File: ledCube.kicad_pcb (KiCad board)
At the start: 2 copper layers, 52 x 22 mm, 13 parts, among them P1 CONN_01X03, P2 CONN_01X02, P3 CONN_01X02, P4 CONN_01X02, P5 CONN_01X02, U1 AL8805W5

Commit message: Generate BOM & Gerber
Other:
- outline, holes or cut-outs redrawn
- board text added: "PWM V+ GND"
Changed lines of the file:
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@@
     (links 22)
     (no_connects 0)
-    (area 118.899999 88.899999 141.100001 111.100001)
+    (area 88.899999 86.925 144.033334 112.175)
     (thickness 1.6)
-    (drawings 14)
+    (drawings 15)
     (tracks 56)
     (zones 0)
@@
     (pad_to_mask_clearance 0.2)
     (aux_axis_origin 0 0)
-    (visible_elements FFFFFF7F)
+    (visible_elements 7FFFFFFF)
     (pcbplotparams
-      (layerselection 0x00030_80000001)
+      (layerselection 0x010f0_80000001)
       (usegerberextensions false)
       (excludeedgelayer true)
@@
       (outputformat 1)
       (mirror false)
-      (drillshape 1)
+      (drillshape 0)
       (scaleselection 1)
-      (outputdirectory ""))
+      (outputdirectory gerber/))
   )
   (net 0 "")
@@
     )
   )
+  (gr_text "PWM V+ GND" (at 133.1 105.3) (layer B.SilkS)
+    (effects (font (size 1 1) (thickness 0.25)) (justify mirror))
+  )
   (gr_text "BlueSink\nLedCube v.0" (at 94.2 105.2) (layer F.SilkS)
     (effects (font (size 1 1) (thickness 0.25) italic))
@@
   (gr_line (start 89 111) (end 111 111) (layer Edge.Cuts) (width 0.2))
   (gr_line (start 89 89) (end 89 111) (layer Edge.Cuts) (width 0.2))
-  (gr_circle (center 100 100) (end 100 96) (layer Edge.Cuts) (width 0.15))
+  (gr_circle (center 100 100) (end 100 95.9) (layer Edge.Cuts) (width 0.15))
   (gr_line (start 89 89) (end 111 89) (layer Edge.Cuts) (width 0.2))
   (gr_line (start 123.75 95) (end 119 95) (layer Edge.Cuts) (width 0.2))

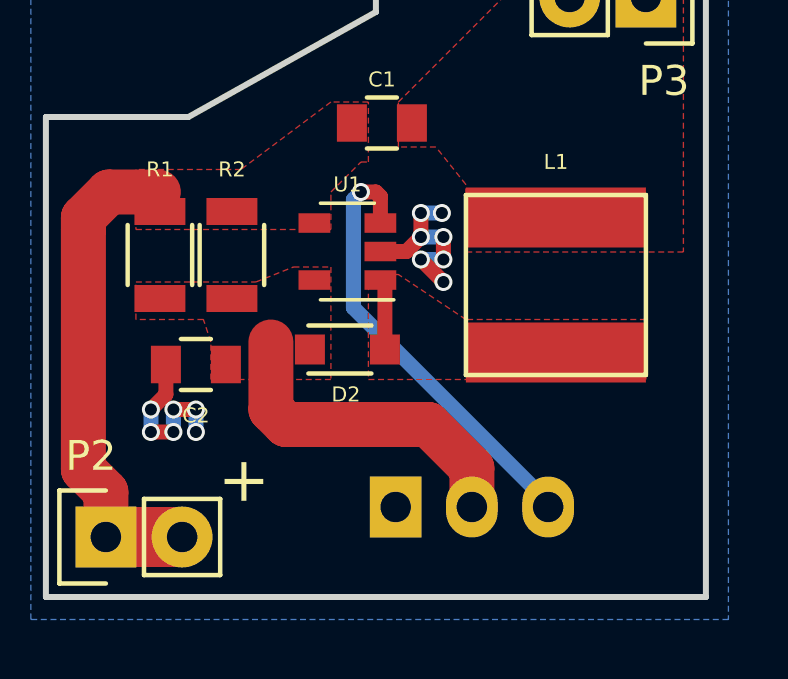
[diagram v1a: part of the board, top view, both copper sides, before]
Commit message: pull down PWM line
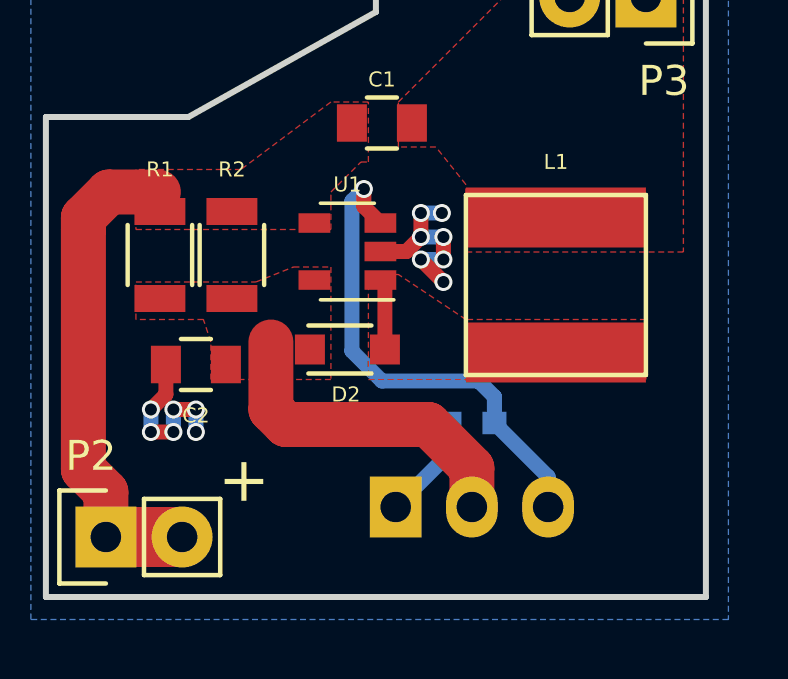
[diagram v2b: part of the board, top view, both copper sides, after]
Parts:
- added R3: 10k, Capacitors_SMD:C_0603, B.Cu at (133.2, 105.2)
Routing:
- net GND: track 11.8 -> 15.4 mm
- net /PWM: track 14.9 -> 16.9 mm
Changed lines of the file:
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@@
-(kicad_pcb (version 4) (host pcbnew 4.0.4-stable)
+(kicad_pcb (version 20160815) (host pcbnew "(2016-12-22 revision d365dc5)-makepkg")
   (general
-    (links 22)
+    (links 24)
     (no_connects 0)
-    (area 88.899999 86.925 144.033334 112.175)
+    (area 88.899999 88.899999 141.100001 111.100001)
     (thickness 1.6)
     (drawings 15)
-    (tracks 56)
+    (tracks 62)
     (zones 0)
-    (modules 13)
+    (modules 14)
     (nets 9)
   )
   (page A4)
   (layers
-    (0 F.Cu signal)
-    (31 B.Cu signal)
+    (0 F.Cu signal hide)
+    (31 B.Cu signal hide)
     (32 B.Adhes user)
     (33 F.Adhes user)
@@
       (hpglpenspeed 20)
       (hpglpendiameter 15)
-      (hpglpenoverlay 2)
       (psnegative false)
       (psa4output false)
@@
     (uvia_dia 0.3)
     (uvia_drill 0.1)
+    (diff_pair_gap 0.25)
+    (diff_pair_width 0.2)
     (add_net /LED+/L)
     (add_net /LED+/U)
@@
   (module footprint:inductor_33uH (layer F.Cu)
     (at 136 100.6 270)
-    (fp_text reference L1 (at -4.1 0 360) (layer F.SilkS)
+    (fp_text reference L1 (at -4.1 0) (layer F.SilkS)
       (effects (font (size 0.5 0.5) (thickness 0.125)))
     )
@@
     )
   )
-  (gr_text "PWM V+ GND" (at 133.1 105.3) (layer B.SilkS)
+  (module Capacitors_SMD:C_0603 (layer B.Cu)
+    (at 133.2 105.2 180)
+    (descr "Capacitor SMD 0603, reflow soldering, AVX (see smccp.pdf)")
+    (tags "capacitor 0603")
+    (attr smd)
+    (fp_text reference R3 (at 0 1.4 180) (layer B.SilkS)
+      (effects (font (size 0.5 0.5) (thickness 0.125)) (justify mirror))
+    )
+    (fp_text value 10k (at 0 -1.9 180) (layer B.Fab) hide
+      (effects (font (size 1 1) (thickness 0.15)) (justify mirror))
+    )
+    (fp_line (start 0.35 -0.6) (end -0.35 -0.6) (layer B.SilkS) (width 0.15))
+    (fp_line (start -0.35 0.6) (end 0.35 0.6) (layer B.SilkS) (width 0.15))
+    (fp_line (start 1.45 0.75) (end 1.45 -0.75) (layer B.CrtYd) (width 0.05))
+    (fp_line (start -1.45 0.75) (end -1.45 -0.75) (layer B.CrtYd) (width 0.05))
+    (fp_line (start -1.45 -0.75) (end 1.45 -0.75) (layer B.CrtYd) (width 0.05))
+    (fp_line (start -1.45 0.75) (end 1.45 0.75) (layer B.CrtYd) (width 0.05))
+    (fp_line (start -0.8 0.4) (end 0.8 0.4) (layer B.Fab) (width 0.15))
+    (fp_line (start 0.8 0.4) (end 0.8 -0.4) (layer B.Fab) (width 0.15))
+    (fp_line (start 0.8 -0.4) (end -0.8 -0.4) (layer B.Fab) (width 0.15))
+    (fp_line (start -0.8 -0.4) (end -0.8 0.4) (layer B.Fab) (width 0.15))
+    (pad 2 smd rect (at 0.75 0 180) (size 0.8 0.75) (layers B.Cu B.Paste B.Mask)
+      (net 2 GND))
+    (pad 1 smd rect (at -0.75 0 180) (size 0.8 0.75) (layers B.Cu B.Paste B.Mask)
+      (net 4 /PWM))
+    (model Capacitors_SMD.3dshapes/C_0603.wrl
+      (at (xyz 0 0 0))
+      (scale (xyz 1 1 1))
+      (rotate (xyz 0 0 0))
+    )
+  )
+  (gr_text "PWM V+ GND" (at 133 110.2) (layer B.SilkS)
     (effects (font (size 1 1) (thickness 0.25)) (justify mirror))
   )
@@
   (segment (start 133.2 106.7) (end 131.75 105.25) (width 1.5) (layer F.Cu) (net 1))
   (segment (start 133.2 108) (end 133.2 106.7) (width 1.5) (layer F.Cu) (net 1))
+  (segment (start 132.45 105.2) (end 132.45 106.21) (width 0.5) (layer B.Cu) (net 2))
+  (segment (start 132.45 106.21) (end 130.66 108) (width 0.5) (layer B.Cu) (net 2))
   (segment (start 131.5 98.2) (end 132.2 98.2) (width 0.5) (layer B.Cu) (net 2))
   (via (at 132.2 98.2) (size 0.6) (drill 0.4) (layers F.Cu B.Cu) (net 2))
@@
   (segment (start 130.3 102.75) (end 130.3 100.584286) (width 0.5) (layer F.Cu) (net 3))
   (segment (start 130.3 100.584286) (end 130.15 100.434286) (width 0.5) (layer F.Cu) (net 3))
-  (segment (start 130 97.5) (end 130.15 97.65) (width 0.5) (layer F.Cu) (net 4))
-  (segment (start 130.15 97.65) (end 130.15 98.534286) (width 0.5) (layer F.Cu) (net 4))
-  (segment (start 129.5 97.5) (end 130 97.5) (width 0.5) (layer F.Cu) (net 4))
-  (segment (start 129.25 101.3576) (end 129.25 97.75) (width 0.5) (layer B.Cu) (net 4))
-  (segment (start 129.25 97.75) (end 129.5 97.5) (width 0.5) (layer B.Cu) (net 4))
-  (via (at 129.5 97.5) (size 0.6) (drill 0.4) (layers F.Cu B.Cu) (net 4))
+  (segment (start 129.6 97.4) (end 129.6 97.984286) (width 0.5) (layer F.Cu) (net 4))
+  (segment (start 129.6 97.984286) (end 130.15 98.534286) (width 0.5) (layer F.Cu) (net 4))
+  (segment (start 129.2 102.8) (end 129.2 97.8) (width 0.5) (layer B.Cu) (net 4))
+  (segment (start 129.2 97.8) (end 129.6 97.4) (width 0.5) (layer B.Cu) (net 4))
+  (via (at 129.6 97.4) (size 0.6) (drill 0.4) (layers F.Cu B.Cu) (net 4))
+  (segment (start 130.2 103.8) (end 129.2 102.8) (width 0.5) (layer B.Cu) (net 4))
+  (segment (start 133.425 103.8) (end 130.2 103.8) (width 0.5) (layer B.Cu) (net 4))
+  (segment (start 133.95 105.2) (end 133.95 104.325) (width 0.5) (layer B.Cu) (net 4))
+  (segment (start 133.95 104.325) (end 133.425 103.8) (width 0.5) (layer B.Cu) (net 4))
+  (segment (start 135.74 108) (end 135.74 106.99) (width 0.5) (layer B.Cu) (net 4))
+  (segment (start 135.74 106.99) (end 133.95 105.2) (width 0.5) (layer B.Cu) (net 4))
   (segment (start 135.74 108) (end 135.74 107.8476) (width 0.5) (layer B.Cu) (net 4))
-  (segment (start 135.74 107.8476) (end 129.25 101.3576) (width 0.5) (layer B.Cu) (net 4))
   (segment (start 121.1 97.5) (end 122.75 97.5) (width 1.5) (layer F.Cu) (net 5))
   (segment (start 120.25 98.75) (end 120.25 98.35) (width 1.5) (layer F.Cu) (net 5))
